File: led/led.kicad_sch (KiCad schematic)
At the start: 38 parts, among them J5 Screw_Terminal_01x05, J6 Screw_Terminal_01x02, J7 Screw_Terminal_01x03, J8 Screw_Terminal_01x03

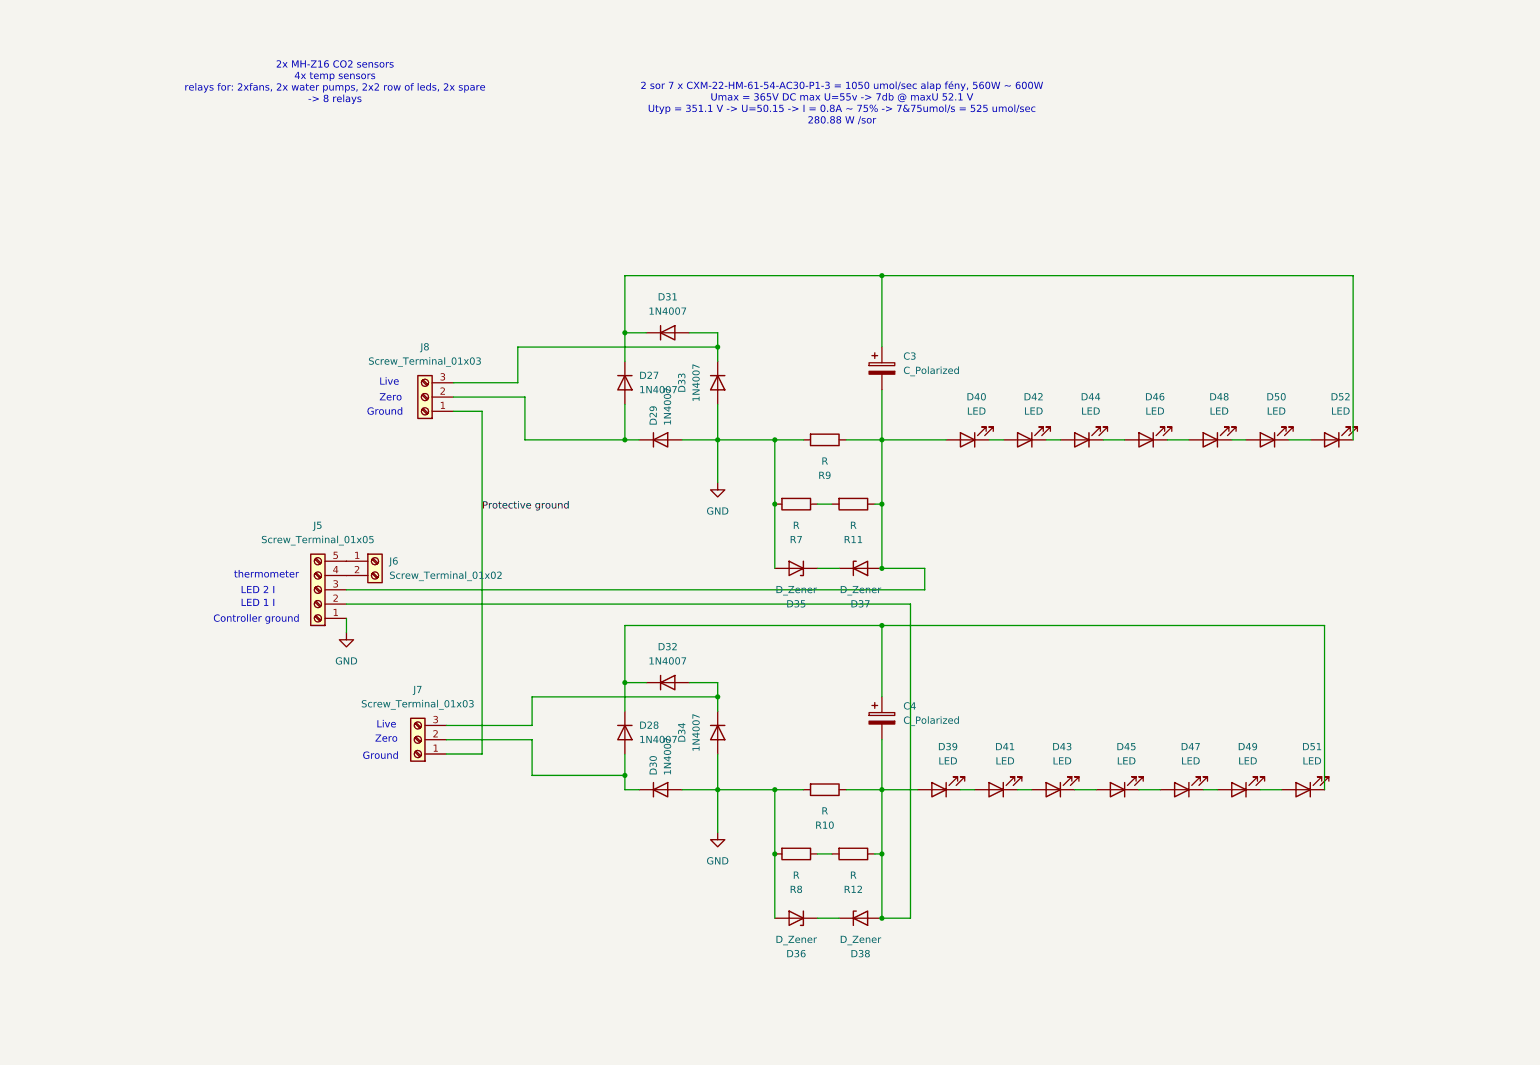
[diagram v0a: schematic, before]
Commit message: made symbols and footprint relative to project
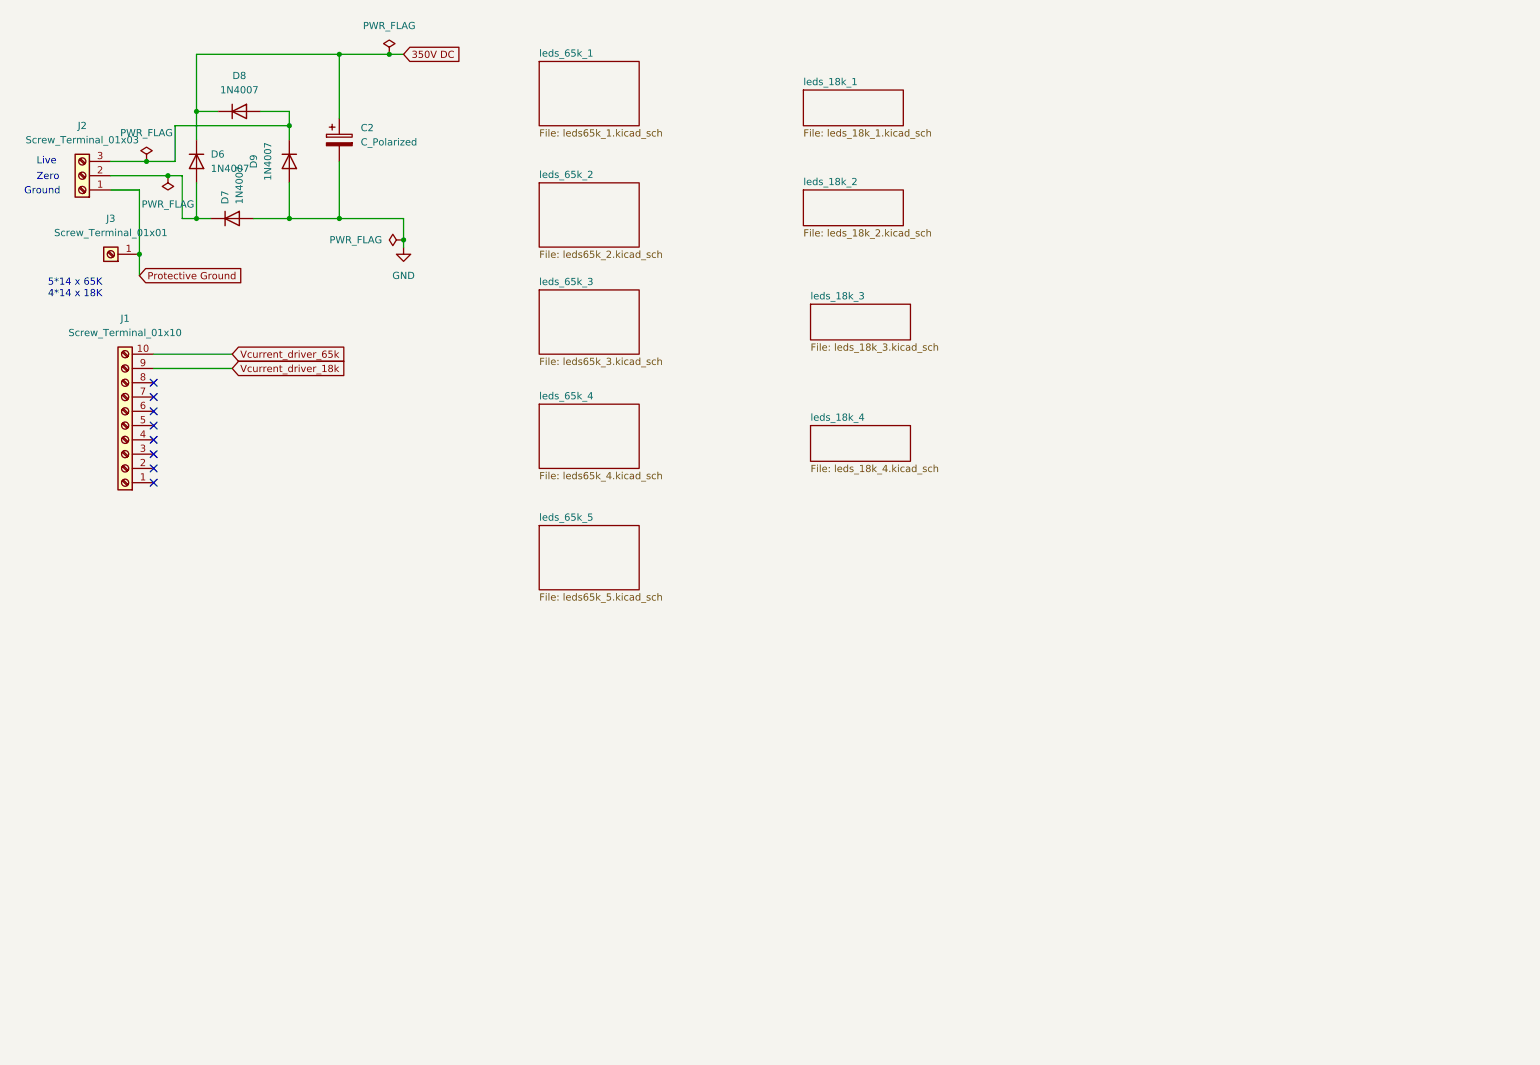
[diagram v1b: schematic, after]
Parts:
- removed C3, C4: C_Polarized, symbol Device:C_Polarized
- removed D27, D28, D29, D30, D31, D32, D33, D34: 1N4007, Diode_THT:D_DO-41_SOD81_P10.16mm_Horizontal, symbol Diode:1N4007
- removed D35, D36, D37, D38: D_Zener, symbol Device:D_Zener
- removed D39, D40, D41, D42, D43, D44, D45, D46, D47, D48, D49, D50, D51, D52: LED, symbol Device:LED
- removed J5: Screw_Terminal_01x05, symbol Connector:Screw_Terminal_01x05
- removed J6: Screw_Terminal_01x02, symbol Connector:Screw_Terminal_01x02
- removed J7, J8: Screw_Terminal_01x03, symbol Connector:Screw_Terminal_01x03
- removed R10, R11, R12, R7, R8, R9: R, symbol Device:R
- added C2: C_Polarized, symbol Device:C_Polarized
- added D6, D7, D8, D9: 1N4007, Diode_THT:D_DO-41_SOD81_P10.16mm_Horizontal, symbol Diode:1N4007
- added J1: Screw_Terminal_01x10, symbol Connector:Screw_Terminal_01x10
- added J2: Screw_Terminal_01x03, symbol Connector:Screw_Terminal_01x03
- added J3: Screw_Terminal_01x01, symbol Connector:Screw_Terminal_01x01
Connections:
- net GND: now also C2.2, D7.2 (A), D9.2 (A)
- new net: D6.2 (A), D7.1 (K), J2.2 (Pin_2)
- new net: D8.2 (A), D9.1 (K), J2.3 (Pin_3)
- new net 350V DC: C2.1, D6.1 (K), D8.1 (K)
- new net Protective Ground: J2.1 (Pin_1), J3.1 (Pin_1)
- new net Vcurrent_driver_18k: J1.9 (Pin_9)
- new net Vcurrent_driver_65k: J1.10 (Pin_10)
- no-connect marks 0 -> 8
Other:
- added sheet leds_18k_1 (leds_18k_1.kicad_sch)
- added sheet leds_18k_2 (leds_18k_2.kicad_sch)
- added sheet leds_18k_3 (leds_18k_3.kicad_sch)
- added sheet leds_18k_4 (leds_18k_4.kicad_sch)
- added sheet leds_65k_1 (leds65k_1.kicad_sch)
- added sheet leds_65k_2 (leds65k_2.kicad_sch)
- added sheet leds_65k_3 (leds65k_3.kicad_sch)
- added sheet leds_65k_4 (leds65k_4.kicad_sch)
- added sheet leds_65k_5 (leds65k_5.kicad_sch)
- note added: "5*14 x 65K 4*14 x 18K"
- note removed: "2 sor 7 x CXM-22-HM-61-54-AC30-P1-3 = 1050 umol/sec alap fény, 560W ~ 600W Umax = 365V DC max U=55v -> 7db @ maxU 52.1 V Utyp = 351.1 V -> U=50.15 -> I = 0.8A ~ 75% -> 7&75umol/s = 525 umol/sec 280.88 W /sor"
- note removed: "2x MH-Z16 CO2 sensors 4x temp sensors relays for: 2xfans, 2x water pumps, 2x2 row of leds, 2x spare -> 8 relays"
- note removed: "Controller ground"
- note removed: "LED 1 I"
- note removed: "LED 2 I"
- note removed: "thermometer"

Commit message: schematics with 5050 leds ready
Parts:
- removed C2: C_Polarized, symbol Device:C_Polarized
- removed D6, D7, D8, D9: 1N4007, Diode_THT:D_DO-41_SOD81_P10.16mm_Horizontal, symbol Diode:1N4007
- removed J1: Screw_Terminal_01x10, symbol Connector:Screw_Terminal_01x10
- added A1: Arduino_Nano_v3.x, Module:Arduino_Nano, symbol MCU_Module:Arduino_Nano_v3.x
- added C1, C2: TAP106K025CRW, Resistor_THT:R_Axial_DIN0204_L3.6mm_D1.6mm_P2.54mm_Vertical, symbol Device:C
- added K5: G6DN-1A_DC4.5, arduino-library:G6DN1ADC45, symbol G6DN-1A_DC4_5:G6DN-1A_DC4.5
- added PS1: IRM-45-12, arduino-library:IRM-45, symbol Converter_ACDC:IRM-60-12
- added Q1, Q3: IRF9540NPBF, Package_TO_SOT_THT:TO-220-3_Vertical, symbol Transistor_FET:IRF9540N
- added Q4: BS170, Package_TO_SOT_THT:TO-92_Inline, symbol Transistor_FET:BS170
- added R10, R11, R2, R7: MFR-25FTE52-100K, Resistor_THT:R_Axial_DIN0204_L3.6mm_D1.6mm_P2.54mm_Vertical, symbol Device:R
- added R12, R3: MF1/4DC1982F, Resistor_THT:R_Axial_DIN0204_L3.6mm_D1.6mm_P2.54mm_Vertical, symbol Device:R
- added R8, R9: MF1/4DCT52R2200F, Resistor_THT:R_Axial_DIN0204_L3.6mm_D1.6mm_P2.54mm_Vertical, symbol Device:R
- added U4: LM7805CT/NOPB, Package_TO_SOT_THT:TO-220-3_Vertical, symbol Regulator_Linear:LM7805_TO220
- J2: footprint (none) -> Connector_Wire:SolderWire-1.5sqmm_1x03_P6mm_D1.7mm_OD3mm; now left out of the parts list
- J3: footprint (none) -> Connector_Wire:SolderWire-1.5sqmm_1x01_D1.7mm_OD3.9mm; now left out of the parts list
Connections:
- net GND: now also A1.29 (GND), A1.4 (GND), C1.2, C2.2, K5.2 (COIL_2), PS1.4 (-Vout), R10.2, R12.2, R3.2, R7.2, U4.2 (GND)
- net Vcurrent_driver_65k: now also C1.1, C2.1, R11.2, R12.1, R2.2, R3.1
- net MAINS_ZERO: now reaches J2.2 (Pin_2)
- net MAINS_ZERO: now also PS1.2 (AC/N)
- net at J2.3 (Pin_3): now also K5.8 (COM), PS1.1 (AC/L)
- new net: Q3.2 (D), R11.1
- new net: Q3.1 (G), R10.1, R9.2
- new net: K5.1 (COIL_1), Q4.3 (S)
- new net: Q1.1 (G), R7.1, R8.2
- new net: Q1.2 (D), R2.1
- new net 18K_ON_1: A1.5 (D2)
- new net 18K_ON_2: A1.6 (D3)
- new net 18K_ON_3: A1.7 (D4)
- new net 18K_ON_4: A1.8 (D5)
- new net 65K_ON_1: A1.9 (D6)
- new net 65K_ON_2: A1.10 (D7)
- new net 65K_ON_3: A1.14 (D11)
- new net 65K_ON_4: A1.15 (D12)
- new net 65K_ON_5: A1.16 (D13)
- new net AREF: A1.18 (AREF)
- new net FAN_RELAY: A1.24 (A5)
- new net HD: A1.22 (A3)
- new net HUMIDITY: A1.19 (A0)
- new net LAMP_RELAY: A1.23 (A4), Q4.2 (G)
- new net MAINS_LIVE: K5.5 (NO)
- new net ONEWIRE: A1.11 (D8)
- new net PUMP_RELAY: A1.25 (A6)
- new net PWM_18K: A1.13 (D10), R9.1
- new net PWM_65K: A1.12 (D9), R8.1
- new net RXD: A1.1 (D1/TX)
- new net TXD: A1.2 (D0/RX)
- new net VALVE_RELAY: A1.26 (A7)
- new net VCC: PS1.3 (+Vout), U4.1 (VI)
- new net VDD: A1.30 (VIN), Q1.3 (S), Q3.3 (S), Q4.1 (D), U4.3 (VO)
- no-connect marks 8 -> 6
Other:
- added sheet Outputs (outputs.kicad_sch)
- sheet leds_18k_1: file leds_18k_1.kicad_sch -> leds18k_1.kicad_sch
- sheet leds_18k_1 ports: added CURRENT_DRIVER_PWM, LEDS_ON; removed none
- sheet leds_18k_2: file leds_18k_2.kicad_sch -> leds18k_1.kicad_sch
- sheet leds_18k_2 ports: added CURRENT_DRIVER_PWM, LEDS_ON; removed none
- sheet leds_18k_3: file leds_18k_3.kicad_sch -> leds18k_1.kicad_sch
- sheet leds_18k_3 ports: added CURRENT_DRIVER_PWM, LEDS_ON; removed none
- sheet leds_18k_4: file leds_18k_4.kicad_sch -> leds18k_1.kicad_sch
- sheet leds_18k_4 ports: added CURRENT_DRIVER_PWM, LEDS_ON; removed none
- sheet leds_65k_1 ports: added CURRENT_DRIVER_PWM, LEDS_ON; removed none
- sheet leds_65k_2: file leds65k_2.kicad_sch -> leds65k_1.kicad_sch
- sheet leds_65k_2 ports: added CURRENT_DRIVER_PWM, LEDS_ON; removed none
- sheet leds_65k_3: file leds65k_3.kicad_sch -> leds65k_1.kicad_sch
- sheet leds_65k_3 ports: added CURRENT_DRIVER_PWM, LEDS_ON; removed none
- sheet leds_65k_4: file leds65k_4.kicad_sch -> leds65k_1.kicad_sch
- sheet leds_65k_4 ports: added CURRENT_DRIVER_PWM, LEDS_ON; removed none
- sheet leds_65k_5: file leds65k_5.kicad_sch -> leds65k_1.kicad_sch
- sheet leds_65k_5 ports: added CURRENT_DRIVER_PWM, LEDS_ON; removed none
- note added: "inputs: - CO2 (rs232) - nedvesség (R) - lámpa hőmérséklet (OneWire) - szekrény hőmérséklet (OneWire) Outputs: - lamp main relay - fan relay - pump relay - valve relay - 5* 65k füzér kapcsoló (FET) - 4* 18k füzér kapcsoló (FET) - 65k áram vezérlés - 18k áram vezérlés"

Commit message: using single and dual top switch current driver circuits
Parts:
- removed C1, C2: TAP106K025CRW, Resistor_THT:R_Axial_DIN0204_L3.6mm_D1.6mm_P2.54mm_Vertical, symbol Device:C
- removed K5: G6DN-1A_DC4.5, arduino-library:G6DN1ADC45, symbol G6DN-1A_DC4_5:G6DN-1A_DC4.5
- removed Q1, Q3: IRF9540NPBF, Package_TO_SOT_THT:TO-220-3_Vertical, symbol Transistor_FET:IRF9540N
- removed Q4: BS170, Package_TO_SOT_THT:TO-92_Inline, symbol Transistor_FET:BS170
- removed R10, R11, R2, R7: MFR-25FTE52-100K, Resistor_THT:R_Axial_DIN0204_L3.6mm_D1.6mm_P2.54mm_Vertical, symbol Device:R
- removed R12, R3: MF1/4DC1982F, Resistor_THT:R_Axial_DIN0204_L3.6mm_D1.6mm_P2.54mm_Vertical, symbol Device:R
- removed R8, R9: MF1/4DCT52R2200F, Resistor_THT:R_Axial_DIN0204_L3.6mm_D1.6mm_P2.54mm_Vertical, symbol Device:R
- added D6, D7, D8, D9: 5A,1kV, Diode_THT:D_DO-41_SOD81_P10.16mm_Horizontal, symbol Diode:1N4007
- added ESMR401VSN102MA50S_3: 1000 uF, arduino-library:CAPPRD1000W180D3550H5250, symbol Device:C_Polarized
- J2: value Screw_Terminal_01x03 -> 01x03
- J3: value Screw_Terminal_01x01 -> 01x01
- PS1: Mouser Part Number (none) -> 709-IRM45-12
- U4: Mouser Part Number (none) -> 926-LM7805CT/NOPB
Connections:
- net 65K_ON_5 is gone; now on net ONEWIRE: A1.16 (D13)
- net ONEWIRE: no longer A1.11 (D8)
- net at J2.3 (Pin_3), PS1.1 (AC/L): now also D6.2 (A), D7.1 (K)
- net 18K_ON_1: no longer names the net of A1.5 (D2)
- net 18K_ON_2 renamed PWM_65K_1
- net 18K_ON_3: no longer names the net of A1.7 (D4)
- net 18K_ON_4 renamed PWM_65K_2
- net 65K_ON_1 renamed PWM_65K_3
- net 65K_ON_2: no longer names the net of A1.10 (D7)
- net 65K_ON_3 renamed PWM_MAINS
- net 65K_ON_4: no longer names the net of A1.15 (D12)
- net LAMP_RELAY: no longer names the net of A1.23 (A4)
- net MAINS_ZERO: no longer names the net of J2.2 (Pin_2), PS1.2 (AC/N)
- net MAINS_ZERO: now also D8.2 (A), D9.1 (K)
- net PWM_18K renamed PWM_18K_2
- net PWM_65K renamed PWM_18K_1
- new net 350V+: ESMR401VSN102MA50S_3.1
- new net 350V-: ESMR401VSN102MA50S_3.2
- new net top_switch_1channel/DC_IN+: D7.2 (A), D9.2 (A)
- new net top_switch_1channel/DC_IN-: D6.1 (K), D8.1 (K)
- no-connect marks 6 -> 12
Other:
- added sheet top_switch1 (top_switch.kicad_sch)
- added sheet top_switch2 (top_switch.kicad_sch)
- added sheet top_switch3 (top_switch.kicad_sch)
- added sheet top_switch4 (top_switch.kicad_sch)
- added sheet top_switch_1channel (top_switch_1_channel.kicad_sch)
- added sheet top_switch_1channel1 (top_switch_1_channel.kicad_sch)
- sheet leds_18k_1 ports: added VDC+, VDC-; removed CURRENT_DRIVER_PWM, LEDS_ON
- sheet leds_18k_2 ports: added VDC+, VDC-; removed CURRENT_DRIVER_PWM, LEDS_ON
- sheet leds_18k_3 ports: added VDC+, VDC-; removed CURRENT_DRIVER_PWM, LEDS_ON
- sheet leds_18k_4 ports: added VDC+, VDC-; removed CURRENT_DRIVER_PWM, LEDS_ON
- sheet leds_65k_1 ports: added VDC+, VDC-; removed CURRENT_DRIVER_PWM, LEDS_ON
- sheet leds_65k_2 ports: added VDC+, VDC-; removed CURRENT_DRIVER_PWM, LEDS_ON
- sheet leds_65k_3 ports: added VDC+, VDC-; removed CURRENT_DRIVER_PWM, LEDS_ON
- sheet leds_65k_4 ports: added VDC+, VDC-; removed CURRENT_DRIVER_PWM, LEDS_ON
- sheet leds_65k_5 ports: added VDC+, VDC-; removed CURRENT_DRIVER_PWM, LEDS_ON
- moved on the sheet: J2, J3, PS1, U4

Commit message: RTC added
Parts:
- added C7, C8: 2p, Capacitor_THT:C_Disc_D3.0mm_W2.0mm_P2.50mm, symbol Device:C
- added C9: 100p, Capacitor_THT:C_Disc_D8.0mm_W5.0mm_P10.00mm, symbol Device:C
- added H1: BAT, arduino-library:BATHLD005THM, symbol BAT-HLD-005-THM:BAT-HLD-005-THM
- added IC7: RTC, Package_DIP:DIP-8_W7.62mm, symbol MCP7940N-I_P:MCP7940N-I_P
- added R14: 1k, Resistor_THT:R_Axial_DIN0207_L6.3mm_D2.5mm_P2.54mm_Vertical, symbol Device:R
- added R15, R16, R17: 100k, Resistor_THT:R_Axial_DIN0204_L3.6mm_D1.6mm_P2.54mm_Vertical, symbol Device:R
- added Y1: 32.768k, Crystal:Crystal_C26-LF_D2.1mm_L6.5mm_Horizontal, symbol Device:Crystal
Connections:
- net FAN_RELAY: now also A1.21 (A2); no longer A1.24 (A5)
- net GND: now also C7.2, C8.2, C9.2, H1.3 (-), IC7.4 (VSS)
- net VDD: now also IC7.8 (VCC), R15.1, R16.1, R17.1
- net INT_1S: now reaches A1.10 (D7)
- net INT_1S: now also IC7.7 (MFP), R17.2
- net SDA: now reaches A1.23 (A4)
- net SDA: now also IC7.5 (SDA), R15.2
- new net: C9.1, H1.1 (+_1), H1.2 (+_2), R14.2
- new net: C8.1, IC7.2 (X2), Y1.1
- new net: C7.1, IC7.1 (X1), Y1.2
- new net: IC7.3 (VBAT), R14.1
- new net SCL: A1.24 (A5), IC7.6 (SCL), R16.2
- no-connect marks 12 -> 9
